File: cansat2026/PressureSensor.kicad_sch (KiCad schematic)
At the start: 2 parts, among them U601 AE-BME280

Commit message: Update: いろいろした
無線変えた
カメラのコネクタ変えた
i2cセンサ変えた
電源変えた:1.2V,3.8V,3.3V
IOエキスパンダ追加
FPGA追加
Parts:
- removed U601: AE-BME280, Project:AE-BME280, symbol Project:AE-BME280
- added C601: 100nF, Capacitor_SMD:C_0402_1005Metric, symbol Device:C
- added U601: MS5611-01BA, Package_LGA:LGA-8_3x5mm_P1.25mm, symbol Sensor_Pressure:MS5611-01BA
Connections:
- net GND: now also C601.2, U601.3 (GND)
- net SCK: now also U601.8 (SCLK)
- net SDA: now also U601.7 (SDI/SDA)
- net VCC: now also C601.1, U601.1 (VDD), U601.2 (PS)
- net at JP601.2 (C): now also U601.4 (CSB), U601.5 (CSB)
- no-connect marks 0 -> 1

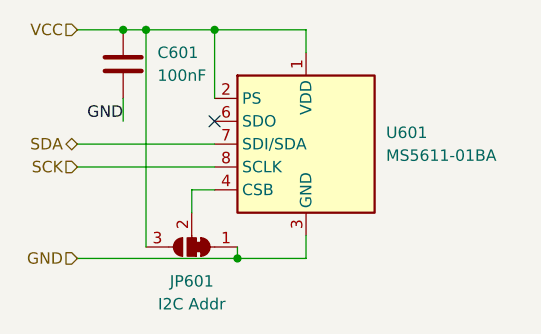
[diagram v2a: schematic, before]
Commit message: Update: いろいろした
GPS変えた
USB追加した
気圧センサ変えた
FPGA変えた
MDにキャパシタ追加した
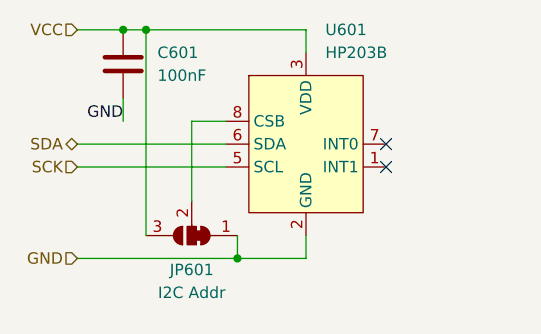
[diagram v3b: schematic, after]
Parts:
- removed U601: MS5611-01BA, Package_LGA:LGA-8_3x5mm_P1.25mm, symbol Sensor_Pressure:MS5611-01BA
- added U601: HP203B, Project:HP203B, symbol Project:HP203B
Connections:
- net GND: now also U601.2 (GND)
- net SCK: now also U601.5 (SCL)
- net SDA: now also U601.6 (SDA)
- net VCC: now also U601.3 (VDD)
- net at JP601.2 (C): now also U601.8 (CSB)
- no-connect marks 1 -> 2
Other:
- moved on the sheet: JP601
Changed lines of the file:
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@@
-	)
-	(junction
-		(at 116.84 76.2)
-		(diameter 0)
-		(color 0 0 0 0)
 	)
 	(junction
@@
 	)
 	(no_connect
-		(at 116.84 86.36)
+		(at 135.89 88.9)
+	)
+	(no_connect
+		(at 135.89 91.44)
 	)
 	(wire
@@
 	(wire
 		(pts
-			(xy 109.22 76.2) (xy 116.84 76.2)
-		)
-		(stroke
-			(width 0)
-			(type default)
-		)
-	)
-	(wire
-		(pts
-			(xy 109.22 76.2) (xy 109.22 100.33)
-		)
-		(stroke
-			(width 0)
-			(type default)
-		)
-	)
-	(wire
-		(pts
-			(xy 101.6 91.44) (xy 116.84 91.44)
+			(xy 109.22 76.2) (xy 127 76.2)
+		)
+		(stroke
+			(width 0)
+			(type default)
+		)
+	)
+	(wire
+		(pts
+			(xy 109.22 76.2) (xy 109.22 99.06)
+		)
+		(stroke
+			(width 0)
+			(type default)
+		)
+	)
+	(wire
+		(pts
+			(xy 101.6 91.44) (xy 118.11 91.44)
 		)
 		(stroke
@@
 	(wire
 		(pts
-			(xy 101.6 88.9) (xy 116.84 88.9)
+			(xy 101.6 88.9) (xy 118.11 88.9)
 		)
 		(stroke
@@
 	(wire
 		(pts
-			(xy 116.84 76.2) (xy 127 76.2)
-		)
-		(stroke
-			(width 0)
-			(type default)
-		)
-	)
-	(wire
-		(pts
-			(xy 114.3 96.52) (xy 114.3 93.98)
-		)
-		(stroke
-			(width 0)
-			(type default)
-		)
-	)
-	(wire
-		(pts
-			(xy 114.3 93.98) (xy 116.84 93.98)
-		)
-		(stroke
-			(width 0)
-			(type default)
-		)
-	)
-	(wire
-		(pts
-			(xy 119.38 100.33) (xy 119.38 101.6)
+			(xy 114.3 86.36) (xy 114.3 95.25)
+		)
+		(stroke
+			(width 0)
+			(type default)
+		)
+	)
+	(wire
+		(pts
+			(xy 119.38 99.06) (xy 119.38 101.6)
 		)
 		(stroke
@@
 	(wire
 		(pts
-			(xy 116.84 76.2) (xy 116.84 83.82)
+			(xy 114.3 86.36) (xy 118.11 86.36)
 		)
 		(stroke
@@
 	)
 	(symbol
-		(lib_id "Sensor_Pressure:MS5611-01BA")
-		(at 127 88.9 0)
-		(unit 1)
-		(body_style 1)
-		(exclude_from_sim no)
-		(in_bom yes)
-		(on_board yes)
-		(in_pos_files yes)
-		(dnp no)
-		(fields_autoplaced yes)
-		(property "Reference" "U601"
-			(at 135.89 87.6299 0)
-			(show_name no)
-			(do_not_autoplace no)
-			(effects
-				(font
-					(size 1.27 1.27)
-				)
-				(justify left)
-			)
-		)
-		(property "Value" "MS5611-01BA"
-			(at 135.89 90.1699 0)
-			(show_name no)
-			(do_not_autoplace no)
-			(effects
-				(font
-					(size 1.27 1.27)
-				)
-				(justify left)
-			)
-		)
-		(property "Footprint" "Package_LGA:LGA-8_3x5mm_P1.25mm"
-			(at 127 88.9 0)
-			(hide yes)
-			(show_name no)
-			(do_not_autoplace no)
-			(effects
-				(font
-					(size 1.27 1.27)
-				)
-			)
-		)
-		(property "Datasheet" "https://www.te.com/commerce/DocumentDelivery/DDEController?Action=srchrtrv&DocNm=MS5611-01BA03&DocType=Data+Sheet&DocLang=English"
-			(at 127 88.9 0)
-			(hide yes)
-			(show_name no)
-			(do_not_autoplace no)
-			(effects
-				(font
-					(size 1.27 1.27)
-				)
-			)
-		)
-		(property "Description" "Barometric pressure sensor, 10cm resolution, 10 to 1200 mbar, I2C and SPI interface up to 20MHz, LGA-8"
-			(at 127 88.9 0)
-			(hide yes)
-			(show_name no)
-			(do_not_autoplace no)
-			(effects
-				(font
-					(size 1.27 1.27)
-				)
-			)
-		)
-		(property "DigiKey Part" ""
-			(at 127 88.9 0)
-			(hide yes)
-			(show_name no)
-			(do_not_autoplace no)
-			(effects
-				(font
-					(size 1.27 1.27)
-				)
-			)
-		)
-		(pin "8"
-		)
-		(pin "2"
-		)
-		(pin "1"
-		)
-		(pin "3"
-		)
-		(pin "5"
-		)
-		(pin "4"
-		)
-		(pin "7"
-		)
-		(pin "6"
-		)
-		(instances
-			(project "cansat2026"
-				(path "/bf092721-05bb-4932-a328-528d8d2db6b5/aa5cb7d0-df1f-4bc0-a855-31204212d19c/fcc9fb91-e115-4885-8021-39aaea5b0ad4"
-					(reference "U601")
-					(unit 1)
-				)
-			)
-		)
-	)
-	(symbol
 		(lib_id "Jumper:SolderJumper_3_Bridged12")
-		(at 114.3 100.33 180)
+		(at 114.3 99.06 180)
 		(unit 1)
 		(body_style 1)
@@
 		(fields_autoplaced yes)
 		(property "Reference" "JP601"
-			(at 114.3 104.14 0)
+			(at 114.3 102.87 0)
 			(show_name no)
 			(do_not_autoplace no)
@@
 		)
 		(property "Value" "I2C Addr"
-			(at 114.3 106.68 0)
+			(at 114.3 105.41 0)
 			(show_name no)
 			(do_not_autoplace no)
@@
 		)
 		(property "Footprint" "Jumper:SolderJumper-3_P1.3mm_Bridged12_RoundedPad1.0x1.5mm_NumberLabels"
-			(at 114.3 100.33 0)
+			(at 114.3 99.06 0)
 			(hide yes)
 			(show_name no)
@@
 		)
 		(property "Datasheet" ""
-			(at 114.3 100.33 0)
+			(at 114.3 99.06 0)
 			(hide yes)
 			(show_name no)
@@
 		)
 		(property "Description" "3-pole Solder Jumper, pins 1+2 closed/bridged"
-			(at 114.3 100.33 0)
+			(at 114.3 99.06 0)
 			(hide yes)
 			(show_name no)
@@
 		)
 		(property "LCSC Part" ""
-			(at 114.3 100.33 90)
+			(at 114.3 99.06 90)
 			(hide yes)
 			(show_name no)
@@
 		)
 		(property "Mouser Part" ""
-			(at 114.3 100.33 90)
+			(at 114.3 99.06 90)
 			(hide yes)
 			(show_name no)
@@
 		)
 		(property "DigiKey Part" ""
-			(at 114.3 100.33 0)
+			(at 114.3 99.06 0)
 			(hide yes)
 			(show_name no)
@@
 					(unit 1)
 				)
+			)
+		)
+	)
+	(symbol
+		(lib_id "Project:HP203B")
+		(at 127 88.9 0)
+		(unit 1)
+		(body_style 1)
+		(exclude_from_sim no)
+		(in_bom yes)
+		(on_board yes)
+		(in_pos_files yes)
+		(dnp no)
+		(fields_autoplaced yes)
+		(property "Reference" "U601"
+			(at 129.1433 76.2 0)
+			(show_name no)
+			(do_not_autoplace no)
+			(effects
+				(font
+					(size 1.27 1.27)
+				)
+				(justify left)
+			)
+		)
+		(property "Value" "HP203B"
+			(at 129.1433 78.74 0)
+			(show_name no)
+			(do_not_autoplace no)
+			(effects
+				(font
+					(size 1.27 1.27)
+				)
+				(justify left)
+			)
+		)
+		(property "Footprint" "Project:HP203B"
+			(at 127 71.12 0)
+			(hide yes)
+			(show_name no)
+			(do_not_autoplace no)
+			(effects
+				(font
+					(size 1.27 1.27)
+				)
+			)
+		)
+		(property "Datasheet" ""
+			(at 127 71.12 0)
+			(hide yes)
+			(show_name no)
+			(do_not_autoplace no)
+			(effects
+				(font
+					(size 1.27 1.27)
+				)
+			)
+		)
+		(property "Description" ""
+			(at 127 71.12 0)
+			(hide yes)
+			(show_name no)
+			(do_not_autoplace no)
+			(effects
+				(font
+					(size 1.27 1.27)
+				)
+			)
+		)
+		(property "LCSC Part" "C138665"
+			(at 127 88.9 0)
+			(hide yes)
+			(show_name no)
+			(do_not_autoplace no)
+			(effects
+				(font
+					(size 1.27 1.27)
+				)
+			)
+		)
+		(pin "4"
+		)
+		(pin "2"
+		)
+		(pin "3"
+		)
+		(pin "5"
+		)
+		(pin "6"
+		)
+		(pin "1"
+		)
+		(pin "8"
+		)
+		(pin "7"
+		)
+		(instances
+			(project "cansat2026"
+				(path "/bf092721-05bb-4932-a328-528d8d2db6b5/aa5cb7d0-df1f-4bc0-a855-31204212d19c/fcc9fb91-e115-4885-8021-39aaea5b0ad4"
+					(reference "U601")
+					(unit 1)
+				)
